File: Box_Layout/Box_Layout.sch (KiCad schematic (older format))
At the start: 32 parts, among them J1 Arduino_Mega_Header, X1 AMP967629, X2 DT04-12P

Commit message: Changes to schematic
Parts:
- removed V? (x2): VarOut, symbol TestBoxLibrary:VarOut
- added DS? (x2): DS3502, symbol TestBoxLibrary:DS3502
- added V? (x2): LM2596_ADJ, symbol TestBoxLibrary:LM2596_ADJ
- J1: symbol w_connectors:Arduino_Mega_Header -> Box_Layout-rescue:Arduino_Mega_Header-w_connectors
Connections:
- wire segments 288 -> 317
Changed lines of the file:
@@
 $EndDescr
 $Comp
-L w_connectors:Arduino_Mega_Header J1
+L Box_Layout-rescue:Arduino_Mega_Header-w_connectors J1
 U 1 1 5FEE4E0E
 P 6150 2350
@@
 Connection ~ 3200 6600
 Wire Wire Line
-	3200 6600 3550 6600
-Wire Wire Line
 	3100 6400 3100 6600
 Wire Wire Line
@@
 	4700 4500 5550 4500
 Connection ~ 4700 2450
-$Comp
-L TestBoxLibrary:VarOut V?
-U 1 1 60AB5ED0
-P 4000 2850
-F 0 "V?" H 3900 3125 50  0000 C CNN
-F 1 "VarOut" H 3900 3034 50  0000 C CNN
-F 2 "" H 4000 2850 50  0001 C CNN
-F 3 "" H 4000 2850 50  0001 C CNN
-	1    4000 2850
-	1    0    0    -1
-$EndComp
-$Comp
-L TestBoxLibrary:VarOut V?
-U 1 1 60AB7D95
-P 4000 3350
-F 0 "V?" H 3900 3625 50  0000 C CNN
-F 1 "VarOut" H 3900 3534 50  0000 C CNN
-F 2 "" H 4000 3350 50  0001 C CNN
-F 3 "" H 4000 3350 50  0001 C CNN
-	1    4000 3350
-	1    0    0    -1
-$EndComp
 Wire Wire Line
 	6300 5900 4700 5900
 Wire Wire Line
 	4700 5900 4700 5000
-Wire Wire Line
-	4700 5000 4450 5000
-Wire Wire Line
-	4450 5000 4450 3300
-Wire Wire Line
-	4450 3300 4200 3300
 Connection ~ 6300 5900
 Wire Wire Line
-	4450 3300 4450 2800
-Wire Wire Line
-	4450 2800 4200 2800
-Connection ~ 4450 3300
-Wire Wire Line
-	4200 3000 4400 3000
-Wire Wire Line
-	4400 3000 4400 3500
-Wire Wire Line
-	4400 3500 4200 3500
-Wire Wire Line
-	3600 2800 3300 2800
-Wire Wire Line
-	3300 2800 3300 3350
-Wire Wire Line
 	2550 3350 3300 3350
 Wire Wire Line
-	3600 3300 3350 3300
-Wire Wire Line
 	3350 3300 3350 3450
 Wire Wire Line
 	2550 3450 3350 3450
 Wire Wire Line
-	3600 3000 3550 3000
-Wire Wire Line
-	3550 3000 3550 3500
-Wire Wire Line
-	3550 3500 3600 3500
-Wire Wire Line
-	4200 2900 5300 2900
-Wire Wire Line
-	5300 2900 5300 3650
-Wire Wire Line
-	5300 3650 7200 3650
-Wire Wire Line
-	7200 3650 7200 2000
-Wire Wire Line
-	7200 2000 6650 2000
-Wire Wire Line
-	6700 1950 7250 1950
-Wire Wire Line
-	7250 1950 7250 3700
-Wire Wire Line
-	7250 3700 5250 3700
-Wire Wire Line
-	5250 3700 5250 3400
-Wire Wire Line
-	5250 3400 4200 3400
-Wire Wire Line
 	6650 1900 7300 1900
 Wire Wire Line
-	7300 1900 7300 3750
-Wire Wire Line
-	7300 3750 3450 3750
-Wire Wire Line
-	3450 3750 3450 3550
+	7300 1900 7300 4050
+Wire Wire Line
+	7300 4050 3450 4050
+Wire Wire Line
+	3450 4050 3450 3550
 Wire Wire Line
 	2550 3550 3450 3550
 Wire Wire Line
-	3400 3650 3400 3800
-Wire Wire Line
-	3400 3800 7350 3800
-Wire Wire Line
-	7350 3800 7350 1850
+	3400 3650 3400 4125
+Wire Wire Line
+	3400 4125 7350 4125
+Wire Wire Line
+	7350 4125 7350 1850
 Wire Wire Line
 	7350 1850 6700 1850
@@
 	5650 3900 5350 3900
 Wire Wire Line
-	3350 3750 3350 3850
-Wire Wire Line
-	3350 3850 7400 3850
-Wire Wire Line
-	7400 3850 7400 1800
+	3350 3750 3350 4200
+Wire Wire Line
+	3350 4200 7400 4200
+Wire Wire Line
+	7400 4200 7400 1800
 Wire Wire Line
 	7400 1800 6650 1800
@@
 	5500 4650 5500 2700
 Wire Wire Line
-	7500 1750 7500 3950
-Wire Wire Line
-	7500 3950 3300 3950
-Wire Wire Line
-	3300 3950 3300 3850
+	7500 1750 7500 4275
+Wire Wire Line
+	7500 4275 3300 4275
+Wire Wire Line
+	3300 4275 3300 3850
 Wire Wire Line
 	2550 3850 3300 3850
 Wire Wire Line
 	6700 1750 7500 1750
-Wire Wire Line
-	3550 3500 3550 6600
-Connection ~ 3550 3500
-Connection ~ 3550 6600
-Wire Wire Line
-	3550 6600 5500 6600
-Wire Wire Line
-	4400 3500 4400 4500
-Wire Wire Line
-	4400 4500 4700 4500
-Connection ~ 4400 3500
 Connection ~ 4700 4500
 Wire Wire Line
@@
 Wire Wire Line
 	8250 6350 9000 6350
+$Comp
+L TestBoxLibrary:DS3502 DS?
+U 1 1 60839415
+P 4700 3775
+F 0 "DS?" V 5215 3750 50  0000 C CNN
+F 1 "DS3502" V 5124 3750 50  0000 C CNN
+F 2 "" H 4700 3775 50  0001 C CNN
+F 3 "" H 4700 3775 50  0001 C CNN
+	1    4700 3775
+	0    -1   -1   0
+$EndComp
+$Comp
+L TestBoxLibrary:LM2596_ADJ V?
+U 1 1 6085500A
+P 3975 2675
+F 0 "V?" H 4100 2410 50  0000 C CNN
+F 1 "LM2596_ADJ" H 4100 2501 50  0000 C CNN
+F 2 "" H 3975 2675 50  0001 C CNN
+F 3 "" H 3975 2675 50  0001 C CNN
+	1    3975 2675
+	-1   0    0    1
+$EndComp
+Wire Wire Line
+	3200 6600 5500 6600
+$Comp
+L TestBoxLibrary:DS3502 DS?
+U 1 1 60855D57
+P 4675 3050
+F 0 "DS?" V 5190 3025 50  0000 C CNN
+F 1 "DS3502" V 5099 3025 50  0000 C CNN
+F 2 "" H 4675 3050 50  0001 C CNN
+F 3 "" H 4675 3050 50  0001 C CNN
+	1    4675 3050
+	0    -1   -1   0
+$EndComp
+$Comp
+L TestBoxLibrary:LM2596_ADJ V?
+U 1 1 608EEB19
+P 4000 3300
+F 0 "V?" H 4125 3035 50  0000 C CNN
+F 1 "LM2596_ADJ" H 4125 3126 50  0000 C CNN
+F 2 "" H 4000 3300 50  0001 C CNN
+F 3 "" H 4000 3300 50  0001 C CNN
+	1    4000 3300
+	-1   0    0    1
+$EndComp
+Wire Wire Line
+	4450 3675 3800 3675
+Wire Wire Line
+	3800 3675 3800 3550
+Wire Wire Line
+	3900 3550 3900 3775
+Wire Wire Line
+	3900 3775 4450 3775
+Wire Wire Line
+	4000 3550 4000 3875
+Wire Wire Line
+	4000 3875 4450 3875
+Wire Wire Line
+	4425 3150 3975 3150
+Wire Wire Line
+	3975 3150 3975 2925
+Wire Wire Line
+	4425 3050 3875 3050
+Wire Wire Line
+	3875 3050 3875 2925
+Wire Wire Line
+	4425 2950 3775 2950
+Wire Wire Line
+	3775 2950 3775 2925
+Wire Wire Line
+	4300 3250 4350 3250
+Wire Wire Line
+	4350 3250 4350 2625
+Wire Wire Line
+	4350 2625 4275 2625
+Wire Wire Line
+	4275 2675 4375 2675
+Wire Wire Line
+	4375 2675 4375 3300
+Wire Wire Line
+	4375 3300 4300 3300
+Wire Wire Line
+	4350 4500 4350 3250
+Wire Wire Line
+	4350 4500 4700 4500
+Connection ~ 4350 3250
+Wire Wire Line
+	4375 3300 4375 4350
+Wire Wire Line
+	4375 4350 4225 4350
+Wire Wire Line
+	4225 4350 4225 5000
+Wire Wire Line
+	4225 5000 4700 5000
+Connection ~ 4375 3300
+Wire Wire Line
+	3450 3300 3350 3300
+Wire Wire Line
+	3300 2675 3425 2675
+Wire Wire Line
+	3300 2675 3300 3350
+Wire Wire Line
+	3425 2625 3375 2625
+Wire Wire Line
+	3375 2625 3375 3250
+Wire Wire Line
+	3375 3250 3450 3250
+Wire Wire Line
+	4975 3150 5250 3150
+Wire Wire Line
+	5550 3150 5550 3450
+Connection ~ 5550 3450
+Wire Wire Line
+	5000 3875 5250 3875
+Wire Wire Line
+	5250 3875 5250 3150
+Connection ~ 5250 3150
+Wire Wire Line
+	5250 3150 5550 3150
+Wire Wire Line
+	4975 3250 5150 3250
+Wire Wire Line
+	5150 3250 5150 3575
+Wire Wire Line
+	5150 3975 5000 3975
+Wire Wire Line
+	5150 3250 5150 2600
+Wire Wire Line
+	5150 2600 5650 2600
+Connection ~ 5150 3250
+Wire Wire Line
+	4975 3050 5075 3050
+Wire Wire Line
+	5075 3050 5075 3775
+Wire Wire Line
+	5075 3775 5000 3775
+Connection ~ 5150 3575
+Wire Wire Line
+	5150 3575 5150 3975
+Wire Wire Line
+	5000 3575 5150 3575
+Wire Wire Line
+	5050 3675 5050 2950
+Wire Wire Line
+	5050 2950 4975 2950
+Wire Wire Line
+	5000 3675 5050 3675
+Wire Wire Line
+	5075 3050 5075 800
+Wire Wire Line
+	5075 800  6875 800
+Wire Wire Line
+	6875 800  6875 1200
+Wire Wire Line
+	6875 1200 6700 1200
+Connection ~ 5075 3050
+Wire Wire Line
+	5050 2950 5225 2950
+Wire Wire Line
+	5225 2950 5225 650
+Wire Wire Line
+	5225 650  6925 650
+Wire Wire Line
+	6925 650  6925 1250
+Wire Wire Line
+	6925 1250 6650 1250
+Connection ~ 5050 2950
 $EndSCHEMATC

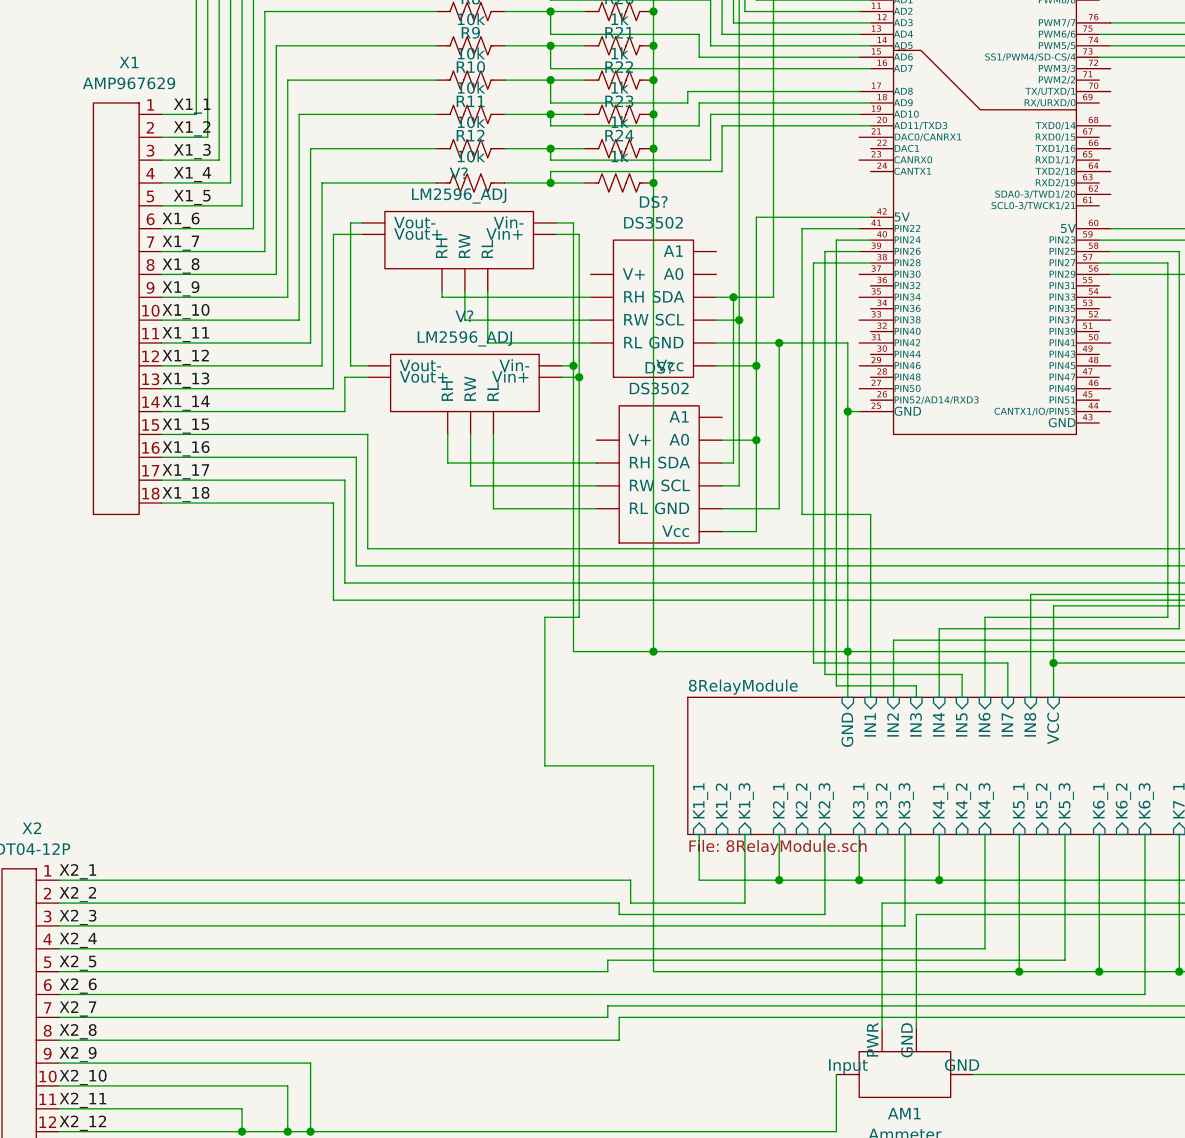
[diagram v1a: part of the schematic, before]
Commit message: Variable Voltage Out Working
Fixed the DS3502 - variable voltage out now works.
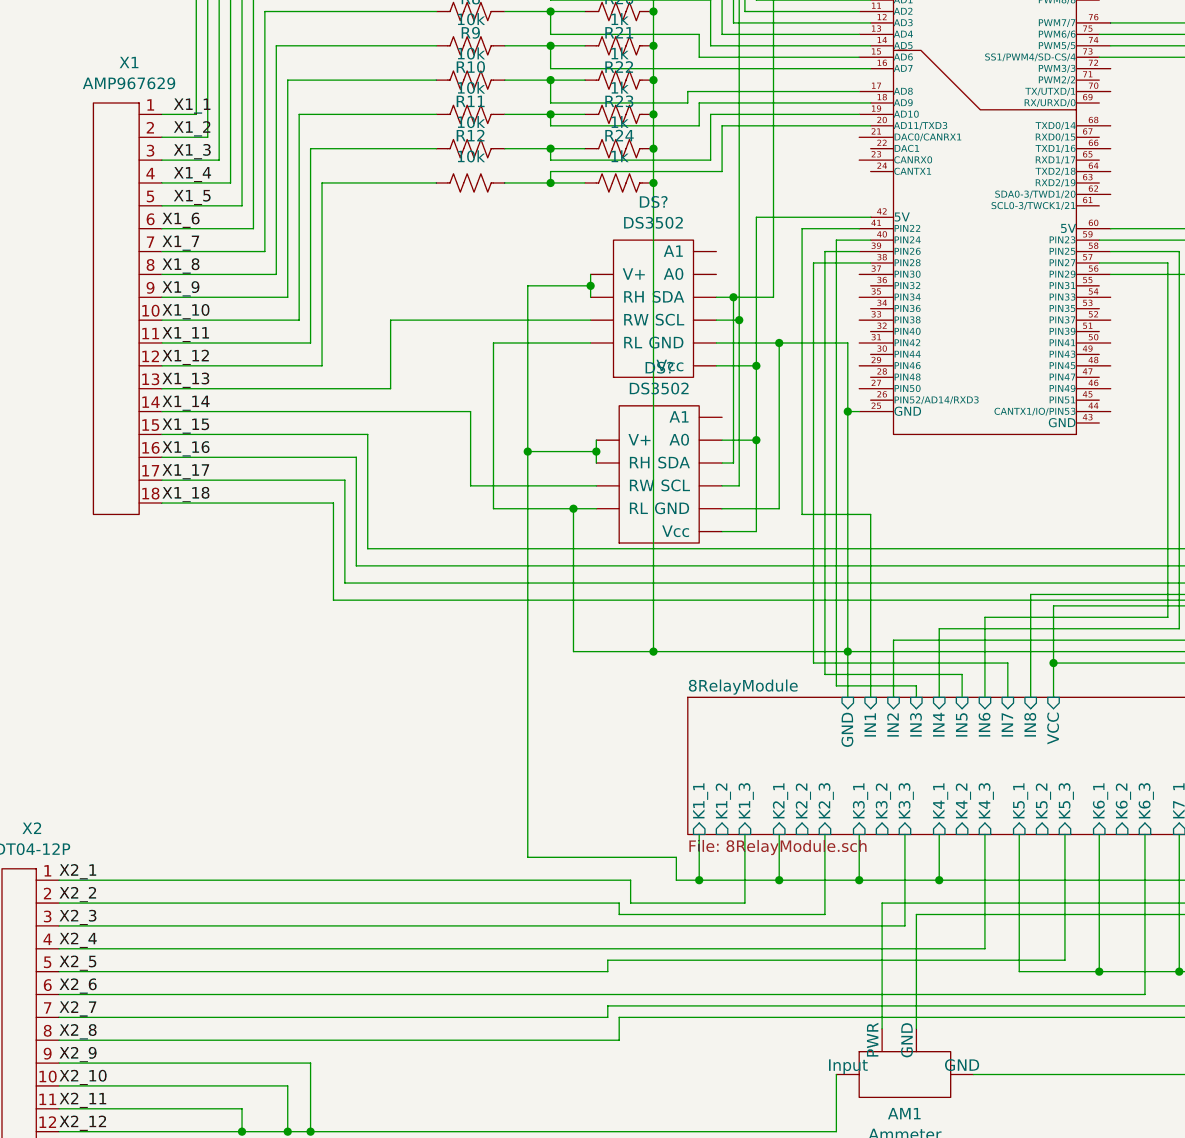
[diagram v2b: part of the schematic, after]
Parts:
- removed V? (x2): LM2596_ADJ, symbol TestBoxLibrary:LM2596_ADJ
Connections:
- net 8RelayModule/K1_1: now also DS?.~ (Vcc), DS?.~ (Vcc)
- net X1_13: now also DS?.~ (Vcc)
- net X1_14: now also DS?.~ (Vcc)
- new net: DS?.~ (Vcc), DS?.~ (Vcc), J1.42 (5V)
- new net: DS?.~ (Vcc), DS?.~ (Vcc), J1.85 (SDA1/TWD0)
- new net: DS?.~ (Vcc), DS?.~ (Vcc), J1.86 (SCL1/TWCK0)
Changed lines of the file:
@@
 Connection ~ 4700 2450
-Wire Wire Line
-	6300 5900 4700 5900
-Wire Wire Line
-	4700 5900 4700 5000
-Connection ~ 6300 5900
-Wire Wire Line
-	2550 3350 3300 3350
-Wire Wire Line
-	3350 3300 3350 3450
-Wire Wire Line
-	2550 3450 3350 3450
 Wire Wire Line
 	6650 1900 7300 1900
@@
 	0    -1   -1   0
 $EndComp
-$Comp
-L TestBoxLibrary:LM2596_ADJ V?
-U 1 1 6085500A
-P 3975 2675
-F 0 "V?" H 4100 2410 50  0000 C CNN
-F 1 "LM2596_ADJ" H 4100 2501 50  0000 C CNN
-F 2 "" H 3975 2675 50  0001 C CNN
-F 3 "" H 3975 2675 50  0001 C CNN
-	1    3975 2675
-	-1   0    0    1
-$EndComp
 Wire Wire Line
 	3200 6600 5500 6600
@@
 	0    -1   -1   0
 $EndComp
-$Comp
-L TestBoxLibrary:LM2596_ADJ V?
-U 1 1 608EEB19
-P 4000 3300
-F 0 "V?" H 4125 3035 50  0000 C CNN
-F 1 "LM2596_ADJ" H 4125 3126 50  0000 C CNN
-F 2 "" H 4000 3300 50  0001 C CNN
-F 3 "" H 4000 3300 50  0001 C CNN
-	1    4000 3300
-	-1   0    0    1
-$EndComp
-Wire Wire Line
-	4450 3675 3800 3675
-Wire Wire Line
-	3800 3675 3800 3550
-Wire Wire Line
-	3900 3550 3900 3775
 Wire Wire Line
 	3900 3775 4450 3775
 Wire Wire Line
-	4000 3550 4000 3875
-Wire Wire Line
-	4000 3875 4450 3875
-Wire Wire Line
-	4425 3150 3975 3150
-Wire Wire Line
-	3975 3150 3975 2925
-Wire Wire Line
-	4425 3050 3875 3050
-Wire Wire Line
-	3875 3050 3875 2925
-Wire Wire Line
-	4425 2950 3775 2950
-Wire Wire Line
-	3775 2950 3775 2925
-Wire Wire Line
-	4300 3250 4350 3250
-Wire Wire Line
-	4350 3250 4350 2625
-Wire Wire Line
-	4350 2625 4275 2625
-Wire Wire Line
-	4275 2675 4375 2675
-Wire Wire Line
-	4375 2675 4375 3300
-Wire Wire Line
-	4375 3300 4300 3300
-Wire Wire Line
-	4350 4500 4350 3250
+	4000 3875 4350 3875
 Wire Wire Line
 	4350 4500 4700 4500
-Connection ~ 4350 3250
-Wire Wire Line
-	4375 3300 4375 4350
-Wire Wire Line
-	4375 4350 4225 4350
-Wire Wire Line
-	4225 4350 4225 5000
-Wire Wire Line
-	4225 5000 4700 5000
-Connection ~ 4375 3300
-Wire Wire Line
-	3450 3300 3350 3300
-Wire Wire Line
-	3300 2675 3425 2675
-Wire Wire Line
-	3300 2675 3300 3350
-Wire Wire Line
-	3425 2625 3375 2625
-Wire Wire Line
-	3375 2625 3375 3250
-Wire Wire Line
-	3375 3250 3450 3250
 Wire Wire Line
 	4975 3150 5250 3150
@@
 	6925 1250 6650 1250
 Connection ~ 5050 2950
+Wire Wire Line
+	4450 3575 4450 3625
+Wire Wire Line
+	4425 2850 4425 2900
+Wire Wire Line
+	4425 3150 4000 3150
+Wire Wire Line
+	4000 3150 4000 3875
+Wire Wire Line
+	4900 5500 4800 5500
+Wire Wire Line
+	4800 5500 4800 5400
+Wire Wire Line
+	4800 5400 4150 5400
+Wire Wire Line
+	4150 5400 4150 3625
+Wire Wire Line
+	4150 3625 4450 3625
+Connection ~ 4900 5500
+Connection ~ 4450 3625
+Wire Wire Line
+	4450 3625 4450 3675
+Wire Wire Line
+	4150 3625 4150 2900
+Wire Wire Line
+	4150 2900 4425 2900
+Connection ~ 4150 3625
+Connection ~ 4425 2900
+Wire Wire Line
+	4425 2900 4425 2950
+Wire Wire Line
+	3900 3775 3900 3450
+Wire Wire Line
+	2550 3450 3900 3450
+Wire Wire Line
+	4425 3050 3550 3050
+Wire Wire Line
+	3550 3050 3550 3350
+Wire Wire Line
+	2550 3350 3550 3350
+Wire Wire Line
+	4350 4500 4350 3875
+Connection ~ 4350 3875
+Wire Wire Line
+	4350 3875 4450 3875
 $EndSCHEMATC
